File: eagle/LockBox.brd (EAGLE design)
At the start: 100 x 80 mm, 19 parts

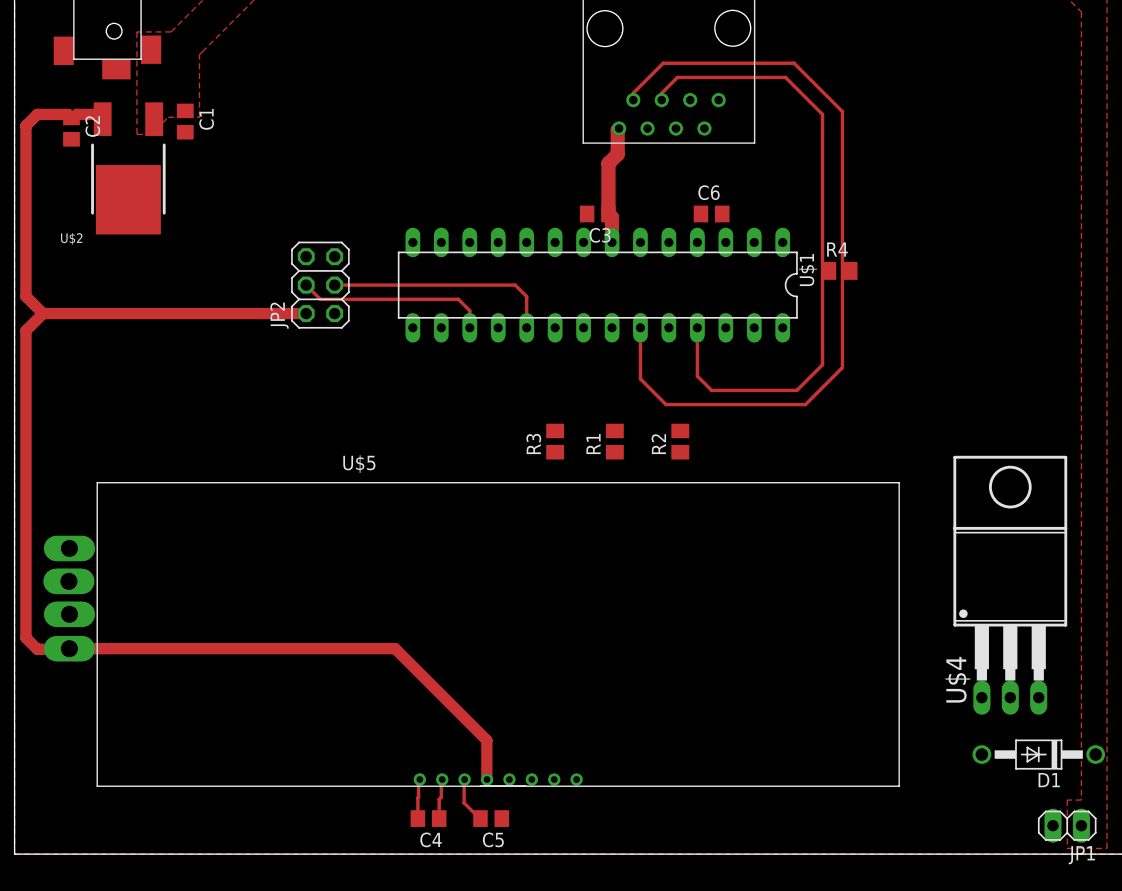
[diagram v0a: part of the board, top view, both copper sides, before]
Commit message: Finished first draft of board layout. I have not ran a DRU yet because I dont have the OSHPARK DRU files.
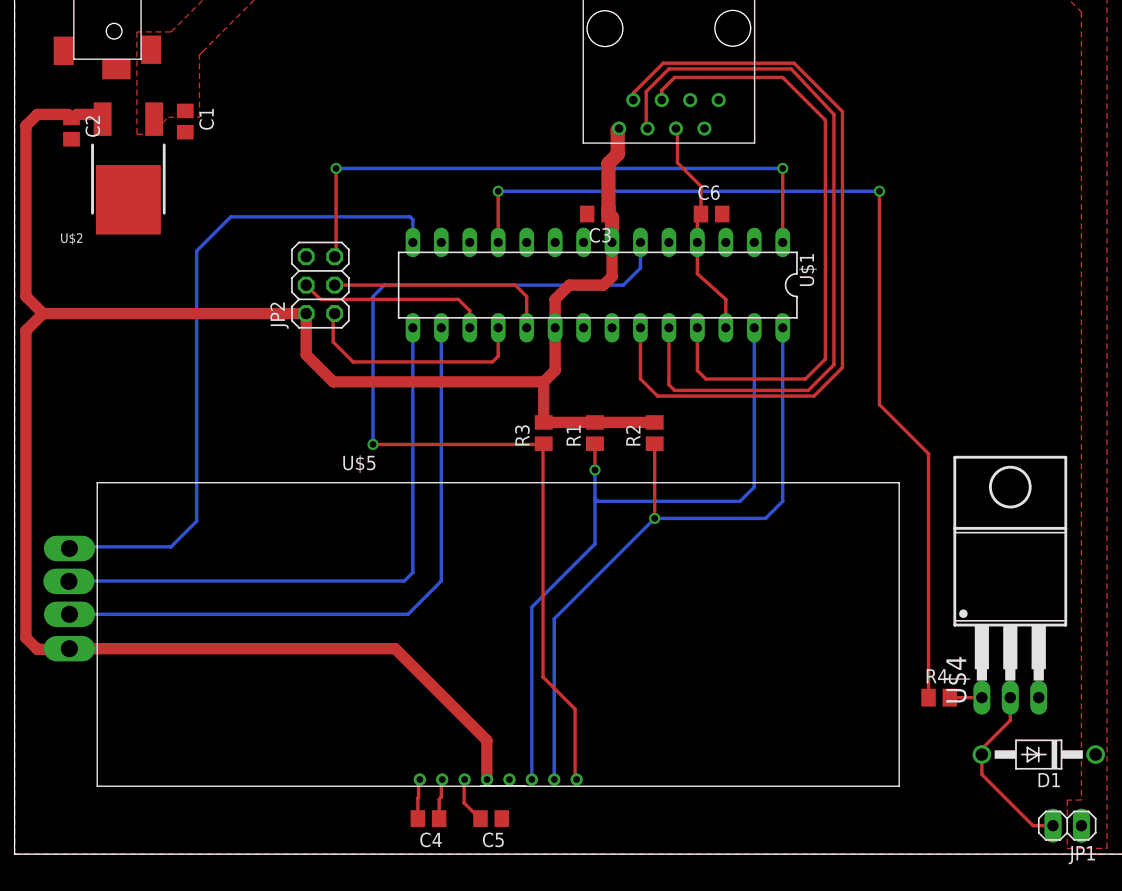
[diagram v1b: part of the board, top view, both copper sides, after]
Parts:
- moved R4 39.1 mm to (82.5, 14.0)
- moved R2 2.41 mm to (57.1, 37.6)
- moved R1 1.93 mm to (51.8, 37.6)
- moved R3 1.27 mm to (47.2, 37.6)
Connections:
- new net N$1: R4.2, U$4.1
- net SOL_EN: no longer R4.2, U$4.1
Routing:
- net !LCD_RST: track 0.00 -> 86.8 mm, vias 0 -> 1
- net SOL_EN: track 0.00 -> 85.6 mm, vias 0 -> 2
- net A1: track 0.00 -> 66.0 mm
- net SDA: track 0.00 -> 61.4 mm, vias 0 -> 1
- net SCL: track 0.00 -> 61.3 mm, vias 0 -> 1
- net EN_RD: track 0.00 -> 59.2 mm
- net EN_BL: track 0.00 -> 57.0 mm
- net 3.3V: track 137.4 -> 193.5 mm
- net !RST: track 0.00 -> 54.4 mm, vias 0 -> 2
- net EN_GR: track 0.00 -> 52.9 mm
- net MISO: track 0.00 -> 20.8 mm
- net START: track 0.00 -> 20.0 mm
- net N$5: track 0.00 -> 16.2 mm
- net N$1: track 0.00 -> 2.86 mm
- net A2: track 56.2 -> 55.2 mm
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
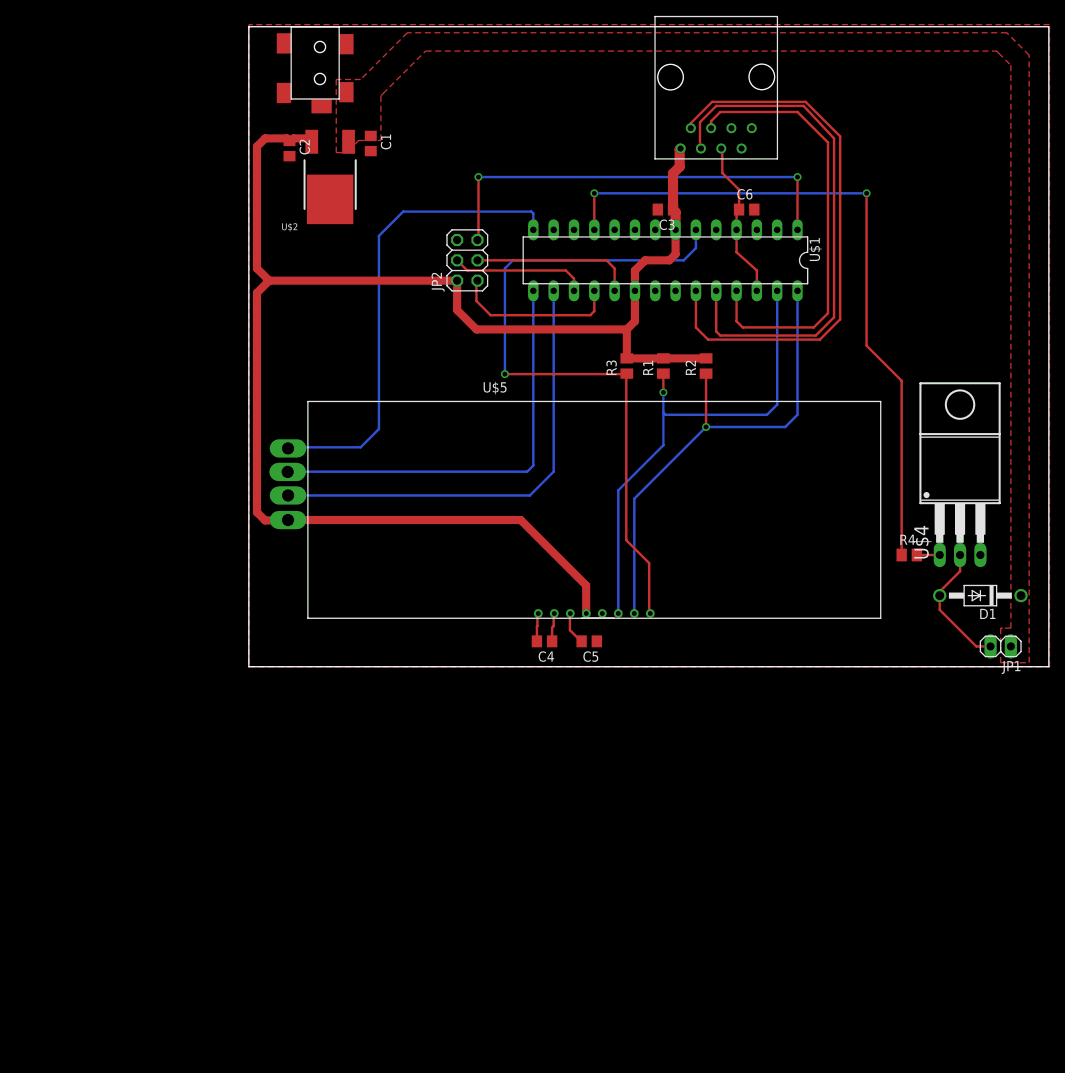
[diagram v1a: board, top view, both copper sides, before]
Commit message: Removed the LCD screen from the .sch and inserted a pin header in its place.
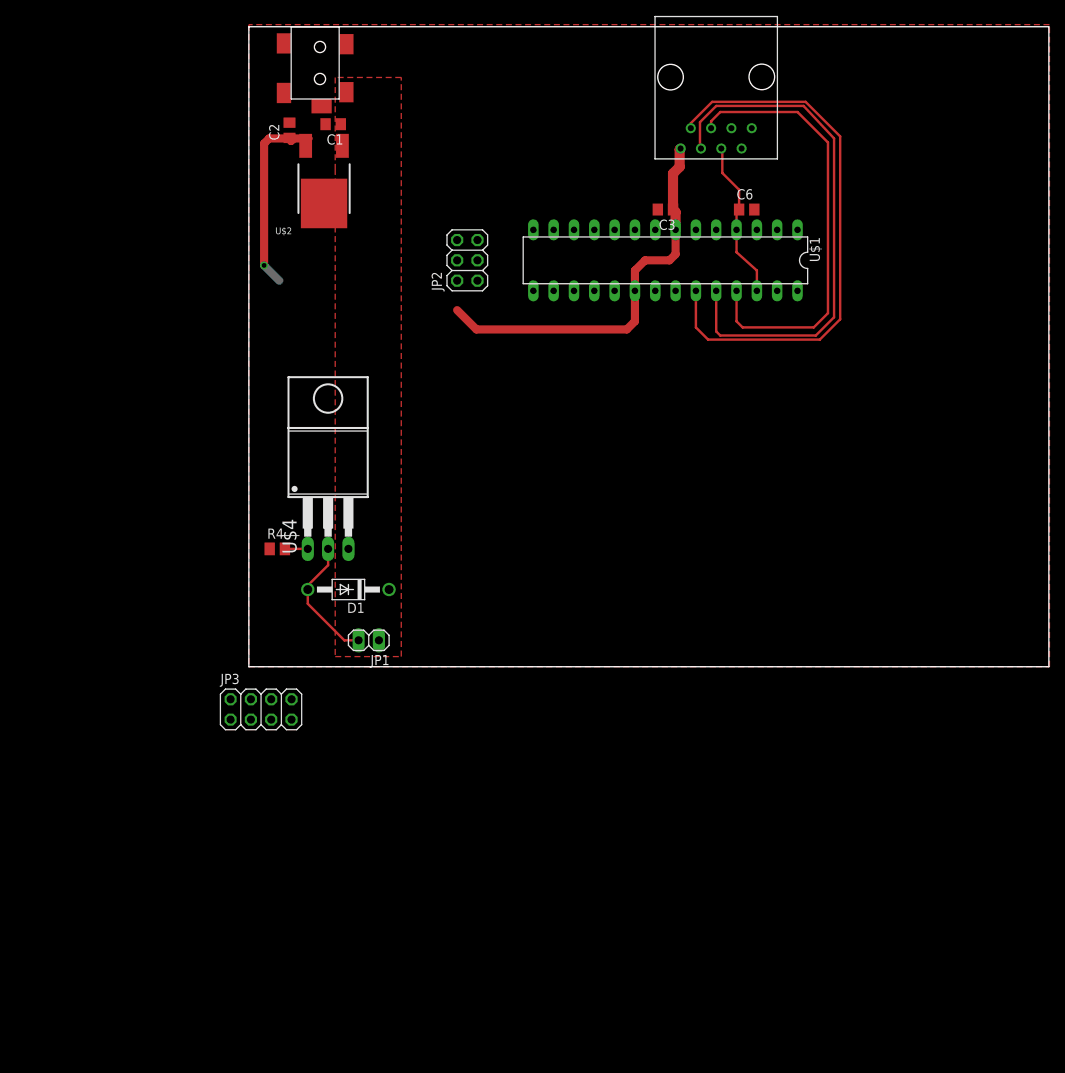
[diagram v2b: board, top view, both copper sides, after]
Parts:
- removed C4, C5: 1uF, LockBox:C0805
- removed R1, R2: 4.7k, LockBox:M0805
- removed R3: 10k, LockBox:M0805
- removed U$5: NHD-C0220BIZ, LockBox:NHD-C0220BIZ-LCD
- added JP3: LCD, LockBox:2X04
- moved D1 79.0 mm to (12.4, 9.65)
- moved JP1 79.0 mm to (15.0, 3.30)
- moved R4 79.0 mm to (3.56, 14.7)
- moved U$4 79.0 mm to (9.91, 26.2)
- moved C1 5.28 mm to (10.5, 67.8), turned to 180 degrees
- moved C2 2.29 mm to (5.08, 67.1), turned to 90 degrees
- moved U$2 0.92 mm to (9.40, 57.9)
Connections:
- removed net !LCD_RST: R3.1, U$1.6, U$5.P$1
- removed net N$2: C4.1, U$5.P$7
- removed net N$3: C4.2, U$5.P$8
- removed net N$4: C5.2, U$5.P$6
- new net LCD_RST: JP3.2, U$1.11
- new net P$1: JP2.2
- net 3.3V: now also JP3.1; no longer JP2.2, R1.2, R2.2, R3.2, U$5.P$5, U$5.P$A
- net EN_BL: now also JP3.3; no longer U$5.P$BK
- net EN_GR: now also JP3.5; no longer U$5.P$GK
- net EN_RD: now also JP3.7; no longer U$5.P$RK
- net GND: now also JP3.8; no longer C5.1, U$5.P$4
- net SCL: now also JP3.4; no longer R2.1, U$5.P$2
- net SDA: now also JP3.6; no longer R1.1, U$5.P$3
- net SOL_EN: now also U$1.6; no longer U$1.11
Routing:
- net 3.3V: track 193.5 -> 74.8 mm, vias 0 -> 1
- net !LCD_RST: track 86.8 -> 0.00 mm, vias 1 -> 0
- net SOL_EN: track 85.6 -> 0.00 mm, vias 2 -> 0
- net SDA: track 61.4 -> 0.00 mm, vias 1 -> 0
- net SCL: track 61.3 -> 0.00 mm, vias 1 -> 0
- net EN_RD: track 59.2 -> 0.00 mm
- net EN_BL: track 57.0 -> 0.00 mm
- net !RST: track 54.4 -> 0.00 mm, vias 2 -> 0
- net EN_GR: track 52.9 -> 0.00 mm
- net MISO: track 20.8 -> 0.00 mm
- net SCK: track 20.4 -> 0.00 mm
- net MOSI: track 17.1 -> 0.00 mm
- net N$4: track 4.15 -> 0.00 mm
- net N$2: track 3.60 -> 0.00 mm
- net N$3: track 3.56 -> 0.00 mm

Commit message: small changes
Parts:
- added C4: 10uF, LockBox:C0805
- added C5: 1uF, LockBox:C0805
- added R1, R2, R3, R8: 10k, LockBox:R0805
- added R10, R9: 4.7k, LockBox:R0805
- added R5: 150, LockBox:R0805
- added R6: 33, LockBox:R0805
- added R7: 27, LockBox:R0805
- added T1, T2, T3: 2N3904, LockBox:TO92-BCE
- moved C1 15.9 mm to (26.4, 66.4), turned to 270 degrees
- moved U$2 11.4 mm to (9.65, 46.5)
- moved U$3 9.15 mm to (18.0, 77.7)
- moved C2 8.42 mm to (13.5, 66.3)
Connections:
- removed net P$1: JP2.2
- new net BLUE: R3.1, U$1.16
- new net GREEN: R2.1, U$1.15
- new net N$10: R7.1, T3.C
- new net N$11: R6.1, T2.C
- new net N$12: R5.1, T1.C
- new net N$6: R1.2, T1.B
- new net N$7: R2.2, T2.B
- new net N$8: R3.2, T3.B
- new net RED: R1.1, U$1.14
- net +12V: now also C4.1, C5.1
- net 3.3V: now also JP2.2, R10.2, R8.2, R9.2
- net EN_BL: now also R7.2; no longer U$1.16
- net EN_GR: now also R6.2; no longer U$1.15
- net EN_RD: now also R5.2; no longer U$1.14
- net GND: now also C4.2, C5.2, T1.E, T2.E, T3.E
- net LCD_RST: now also R8.1
- net SCL: now also R9.1
- net SDA: now also R10.1
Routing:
- net 3.3V: track 74.8 -> 3.52 mm, vias 1 -> 0
- net N$5: track 16.2 -> 0.00 mm
- net N$1: track 2.86 -> 0.00 mm
- removed copper zone on layer 1, net +12V
